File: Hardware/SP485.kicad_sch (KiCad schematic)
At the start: 7 parts, among them J15 WAFER-GH1.25-4PWB, U41 SP3485EN-L/TR

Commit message: 修存档拉线
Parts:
- renumbered C134 to C107, J15 to J17, U41 to U49
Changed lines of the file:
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@@
 		(pin "1"
+		)
+		(instances
+			(project "HPM5E31_ECatDualFOC"
+				(path "/a07e9810-3899-4327-ba8f-f24142a7c70e/0a303857-7f6b-4ab0-b417-2c02e85984ea"
+					(reference "R124")
+					(unit 1)
+				)
+				(path "/a07e9810-3899-4327-ba8f-f24142a7c70e/327c5a00-ae50-48b3-afbf-1a1bb3f19155"
+					(reference "R118")
+					(unit 1)
+				)
+				(path "/a07e9810-3899-4327-ba8f-f24142a7c70e/57eb4dc0-5591-401c-9f34-9dedbfbe09cb"
+					(reference "R121")
+					(unit 1)
+				)
+			)
 		)
 	)
@@
 		(dnp no)
 		(fields_autoplaced yes)
-		(property "Reference" "#PWR0252"
+		(property "Reference" "#PWR0269"
 			(at 104.14 109.22 0)
 			(effects
@@
 		(pin "1"
 		)
+		(instances
+			(project "HPM5E31_ECatDualFOC"
+				(path "/a07e9810-3899-4327-ba8f-f24142a7c70e/0a303857-7f6b-4ab0-b417-2c02e85984ea"
+					(reference "#PWR0281")
+					(unit 1)
+				)
+				(path "/a07e9810-3899-4327-ba8f-f24142a7c70e/327c5a00-ae50-48b3-afbf-1a1bb3f19155"
+					(reference "#PWR0269")
+					(unit 1)
+				)
+				(path "/a07e9810-3899-4327-ba8f-f24142a7c70e/57eb4dc0-5591-401c-9f34-9dedbfbe09cb"
+					(reference "#PWR0275")
+					(unit 1)
+				)
+			)
+		)
 	)
 	(symbol
@@
 		(dnp no)
 		(fields_autoplaced yes)
-		(property "Reference" "#PWR0248"
+		(property "Reference" "#PWR0265"
 			(at 116.84 83.82 0)
 			(effects
@@
 		(pin "1"
 		)
+		(instances
+			(project "HPM5E31_ECatDualFOC"
+				(path "/a07e9810-3899-4327-ba8f-f24142a7c70e/0a303857-7f6b-4ab0-b417-2c02e85984ea"
+					(reference "#PWR0277")
+					(unit 1)
+				)
+				(path "/a07e9810-3899-4327-ba8f-f24142a7c70e/327c5a00-ae50-48b3-afbf-1a1bb3f19155"
+					(reference "#PWR0265")
+					(unit 1)
+				)
+				(path "/a07e9810-3899-4327-ba8f-f24142a7c70e/57eb4dc0-5591-401c-9f34-9dedbfbe09cb"
+					(reference "#PWR0271")
+					(unit 1)
+				)
+			)
+		)
 	)
 	(symbol
@@
 		(pin "2"
 		)
+		(instances
+			(project "HPM5E31_ECatDualFOC"
+				(path "/a07e9810-3899-4327-ba8f-f24142a7c70e/0a303857-7f6b-4ab0-b417-2c02e85984ea"
+					(reference "R125")
+					(unit 1)
+				)
+				(path "/a07e9810-3899-4327-ba8f-f24142a7c70e/327c5a00-ae50-48b3-afbf-1a1bb3f19155"
+					(reference "R119")
+					(unit 1)
+				)
+				(path "/a07e9810-3899-4327-ba8f-f24142a7c70e/57eb4dc0-5591-401c-9f34-9dedbfbe09cb"
+					(reference "R122")
+					(unit 1)
+				)
+			)
+		)
 	)
 	(symbol
@@
 		(dnp no)
 		(fields_autoplaced yes)
-		(property "Reference" "U41"
+		(property "Reference" "U49"
 			(at 105.41 81.28 0)
 			(effects
@@
 		(pin "1"
 		)
+		(instances
+			(project "HPM5E31_ECatDualFOC"
+				(path "/a07e9810-3899-4327-ba8f-f24142a7c70e/0a303857-7f6b-4ab0-b417-2c02e85984ea"
+					(reference "U51")
+					(unit 1)
+				)
+				(path "/a07e9810-3899-4327-ba8f-f24142a7c70e/327c5a00-ae50-48b3-afbf-1a1bb3f19155"
+					(reference "U49")
+					(unit 1)
+				)
+				(path "/a07e9810-3899-4327-ba8f-f24142a7c70e/57eb4dc0-5591-401c-9f34-9dedbfbe09cb"
+					(reference "U50")
+					(unit 1)
+				)
+			)
+		)
 	)
 	(symbol
@@
 		(pin "1"
 		)
+		(instances
+			(project "HPM5E31_ECatDualFOC"
+				(path "/a07e9810-3899-4327-ba8f-f24142a7c70e/0a303857-7f6b-4ab0-b417-2c02e85984ea"
+					(reference "L7")
+					(unit 1)
+				)
+				(path "/a07e9810-3899-4327-ba8f-f24142a7c70e/327c5a00-ae50-48b3-afbf-1a1bb3f19155"
+					(reference "L5")
+					(unit 1)
+				)
+				(path "/a07e9810-3899-4327-ba8f-f24142a7c70e/57eb4dc0-5591-401c-9f34-9dedbfbe09cb"
+					(reference "L6")
+					(unit 1)
+				)
+			)
+		)
 	)
 	(symbol
@@
 		(pin "2"
 		)
+		(instances
+			(project "HPM5E31_ECatDualFOC"
+				(path "/a07e9810-3899-4327-ba8f-f24142a7c70e/0a303857-7f6b-4ab0-b417-2c02e85984ea"
+					(reference "R123")
+					(unit 1)
+				)
+				(path "/a07e9810-3899-4327-ba8f-f24142a7c70e/327c5a00-ae50-48b3-afbf-1a1bb3f19155"
+					(reference "R117")
+					(unit 1)
+				)
+				(path "/a07e9810-3899-4327-ba8f-f24142a7c70e/57eb4dc0-5591-401c-9f34-9dedbfbe09cb"
+					(reference "R120")
+					(unit 1)
+				)
+			)
+		)
 	)
 	(symbol
@@
 		(dnp no)
 		(fields_autoplaced yes)
-		(property "Reference" "#PWR0251"
+		(property "Reference" "#PWR0268"
 			(at 130.81 109.22 0)
 			(effects
@@
 		(pin "1"
 		)
+		(instances
+			(project "HPM5E31_ECatDualFOC"
+				(path "/a07e9810-3899-4327-ba8f-f24142a7c70e/0a303857-7f6b-4ab0-b417-2c02e85984ea"
+					(reference "#PWR0280")
+					(unit 1)
+				)
+				(path "/a07e9810-3899-4327-ba8f-f24142a7c70e/327c5a00-ae50-48b3-afbf-1a1bb3f19155"
+					(reference "#PWR0268")
+					(unit 1)
+				)
+				(path "/a07e9810-3899-4327-ba8f-f24142a7c70e/57eb4dc0-5591-401c-9f34-9dedbfbe09cb"
+					(reference "#PWR0274")
+					(unit 1)
+				)
+			)
+		)
 	)
 	(symbol
@@
 		(dnp no)
 		(fields_autoplaced yes)
-		(property "Reference" "C134"
+		(property "Reference" "C107"
 			(at 105.41 101.6 0)
 			(effects
@@
 		(pin "1"
 		)
+		(instances
+			(project "HPM5E31_ECatDualFOC"
+				(path "/a07e9810-3899-4327-ba8f-f24142a7c70e/0a303857-7f6b-4ab0-b417-2c02e85984ea"
+					(reference "C109")
+					(unit 1)
+				)
+				(path "/a07e9810-3899-4327-ba8f-f24142a7c70e/327c5a00-ae50-48b3-afbf-1a1bb3f19155"
+					(reference "C107")
+					(unit 1)
+				)
+				(path "/a07e9810-3899-4327-ba8f-f24142a7c70e/57eb4dc0-5591-401c-9f34-9dedbfbe09cb"
+					(reference "C108")
+					(unit 1)
+				)
+			)
+		)
 	)
 	(symbol
@@
 		(dnp no)
 		(fields_autoplaced yes)
-		(property "Reference" "#PWR0250"
+		(property "Reference" "#PWR0267"
 			(at 171.45 106.68 0)
 			(effects
@@
 		(pin "1"
 		)
+		(instances
+			(project "HPM5E31_ECatDualFOC"
+				(path "/a07e9810-3899-4327-ba8f-f24142a7c70e/0a303857-7f6b-4ab0-b417-2c02e85984ea"
+					(reference "#PWR0279")
+					(unit 1)
+				)
+				(path "/a07e9810-3899-4327-ba8f-f24142a7c70e/327c5a00-ae50-48b3-afbf-1a1bb3f19155"
+					(reference "#PWR0267")
+					(unit 1)
+				)
+				(path "/a07e9810-3899-4327-ba8f-f24142a7c70e/57eb4dc0-5591-401c-9f34-9dedbfbe09cb"
+					(reference "#PWR0273")
+					(unit 1)
+				)
+			)
+		)
 	)
 	(symbol
@@
 		(dnp no)
 		(fields_autoplaced yes)
-		(property "Reference" "#PWR0253"
+		(property "Reference" "#PWR0270"
 			(at 116.84 109.22 0)
 			(effects
@@
 		(pin "1"
 		)
+		(instances
+			(project "HPM5E31_ECatDualFOC"
+				(path "/a07e9810-3899-4327-ba8f-f24142a7c70e/0a303857-7f6b-4ab0-b417-2c02e85984ea"
+					(reference "#PWR0282")
+					(unit 1)
+				)
+				(path "/a07e9810-3899-4327-ba8f-f24142a7c70e/327c5a00-ae50-48b3-afbf-1a1bb3f19155"
+					(reference "#PWR0270")
+					(unit 1)
+				)
+				(path "/a07e9810-3899-4327-ba8f-f24142a7c70e/57eb4dc0-5591-401c-9f34-9dedbfbe09cb"
+					(reference "#PWR0276")
+					(unit 1)
+				)
+			)
+		)
 	)
 	(symbol
@@
 		(dnp no)
 		(fields_autoplaced yes)
-		(property "Reference" "J15"
+		(property "Reference" "J17"
 			(at 179.07 90.5255 0)
 			(effects
@@
 		(pin "3"
 		)
+		(instances
+			(project "HPM5E31_ECatDualFOC"
+				(path "/a07e9810-3899-4327-ba8f-f24142a7c70e/0a303857-7f6b-4ab0-b417-2c02e85984ea"
+					(reference "J19")
+					(unit 1)
+				)
+				(path "/a07e9810-3899-4327-ba8f-f24142a7c70e/327c5a00-ae50-48b3-afbf-1a1bb3f19155"
+					(reference "J17")
+					(unit 1)
+				)
+				(path "/a07e9810-3899-4327-ba8f-f24142a7c70e/57eb4dc0-5591-401c-9f34-9dedbfbe09cb"
+					(reference "J18")
+					(unit 1)
+				)
+			)
+		)
 	)
 	(symbol
@@
 		(dnp no)
 		(fields_autoplaced yes)
-		(property "Reference" "#PWR0249"
+		(property "Reference" "#PWR0266"
 			(at 171.45 91.44 0)
 			(effects
@@
 		(pin "1"
 		)
-	)
+		(instances
+			(project "HPM5E31_ECatDualFOC"
+				(path "/a07e9810-3899-4327-ba8f-f24142a7c70e/0a303857-7f6b-4ab0-b417-2c02e85984ea"
+					(reference "#PWR0278")
+					(unit 1)
+				)
+				(path "/a07e9810-3899-4327-ba8f-f24142a7c70e/327c5a00-ae50-48b3-afbf-1a1bb3f19155"
+					(reference "#PWR0266")
+					(unit 1)
+				)
+				(path "/a07e9810-3899-4327-ba8f-f24142a7c70e/57eb4dc0-5591-401c-9f34-9dedbfbe09cb"
+					(reference "#PWR0272")
+					(unit 1)
+				)
+			)
+		)
+	)

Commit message: 拉线
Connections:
- net 485+: now reaches J17.2 (Pin_2), L5.2
- net 485-: now reaches J17.3 (Pin_3), L5.3
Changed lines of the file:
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@@
+		)
+	)
+	(label "485-"
+		(at 163.83 93.98 0)
+		(effects
+			(font
+				(size 1.27 1.27)
+			)
+			(justify left bottom)
 		)
 	)
@@
 		(effects
 			(font
+				(size 1.27 1.27)
+			)
+			(justify left bottom)
+		)
+	)
+	(label "485+"
+		(at 163.83 88.9 0)
+		(effects
+			(font

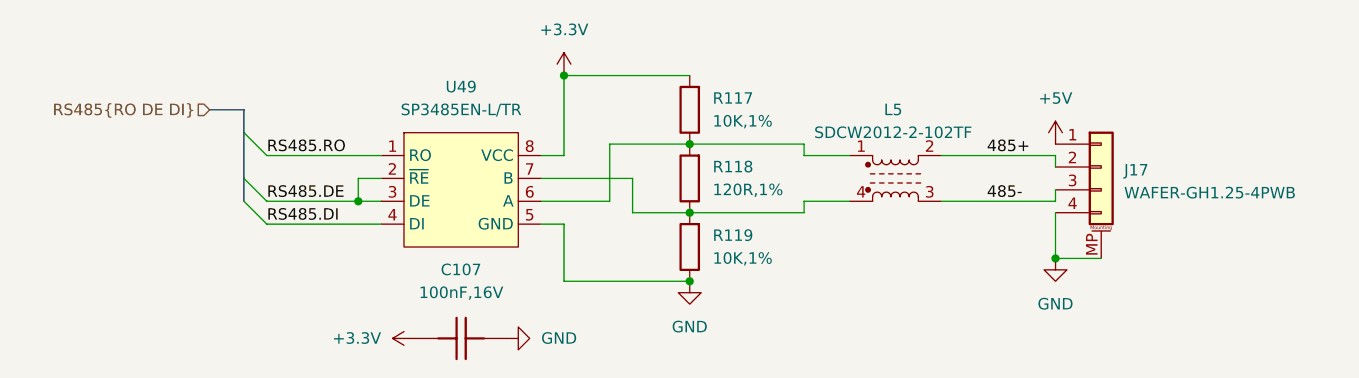
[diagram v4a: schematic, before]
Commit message: PCB：风扇增加控制IO，泄放驱动增加使能引脚，485编码器电源接入控制
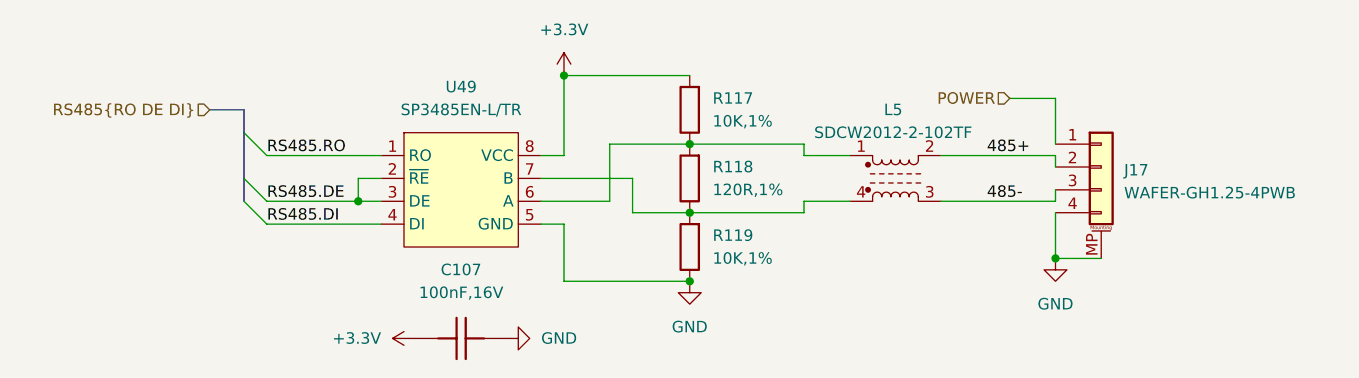
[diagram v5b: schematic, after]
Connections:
- net +5V renamed POWER
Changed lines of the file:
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@@
+	(wire
+		(pts
+			(xy 171.45 87.63) (xy 171.45 82.55)
+		)
+		(stroke
+			(width 0)
+			(type default)
+		)
+	)
 	(wire
 		(pts
 			(xy 121.92 93.98) (xy 121.92 87.63)
+		)
+		(stroke
+			(width 0)
+			(type default)
+		)
+	)
+	(wire
+		(pts
+			(xy 166.37 82.55) (xy 171.45 82.55)
 		)
 		(stroke
@@
 		(shape input)
 		(at 77.47 83.82 180)
+		(effects
+			(font
+				(size 1.27 1.27)
+			)
+			(justify right)
+		)
+	)
+	(hierarchical_label "POWER"
+		(shape input)
+		(at 166.37 82.55 180)
 		(effects
 			(font
@@
 					(unit 1)
 				)
-			)
-		)
-	)
-	(symbol
-		(lib_id "power:+5V")
-		(at 171.45 87.63 0)
-		(unit 1)
-		(exclude_from_sim no)
-		(in_bom yes)
-		(on_board yes)
-		(dnp no)
-		(fields_autoplaced yes)
-		(property "Reference" "#PWR0266"
-			(at 171.45 91.44 0)
-			(effects
-				(font
-					(size 1.27 1.27)
-				)
-				(hide yes)
-			)
-		)
-		(property "Value" "+5V"
-			(at 171.45 82.55 0)
-			(effects
-				(font
-					(size 1.27 1.27)
-				)
-			)
-		)
-		(property "Footprint" ""
-			(at 171.45 87.63 0)
-			(effects
-				(font
-					(size 1.27 1.27)
-				)
-				(hide yes)
-			)
-		)
-		(property "Datasheet" ""
-			(at 171.45 87.63 0)
-			(effects
-				(font
-					(size 1.27 1.27)
-				)
-				(hide yes)
-			)
-		)
-		(property "Description" "Power symbol creates a global label with name \"+5V\""
-			(at 171.45 87.63 0)
-			(effects
-				(font
-					(size 1.27 1.27)
-				)
-				(hide yes)
-			)
-		)
-		(pin "1"
-		)
-		(instances
-			(project "HPM5E31_ECatDualFOC"
-				(path "/a07e9810-3899-4327-ba8f-f24142a7c70e/0a303857-7f6b-4ab0-b417-2c02e85984ea"
-					(reference "#PWR0278")
-					(unit 1)
-				)
-				(path "/a07e9810-3899-4327-ba8f-f24142a7c70e/327c5a00-ae50-48b3-afbf-1a1bb3f19155"
-					(reference "#PWR0266")
-					(unit 1)
-				)
-				(path "/a07e9810-3899-4327-ba8f-f24142a7c70e/57eb4dc0-5591-401c-9f34-9dedbfbe09cb"
-					(reference "#PWR0272")
-					(unit 1)
-				)
